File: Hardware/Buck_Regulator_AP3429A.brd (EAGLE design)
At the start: 160 x 100 mm, 23 parts, among them J2 POWER_JACKPOWER_JACK_SLOT

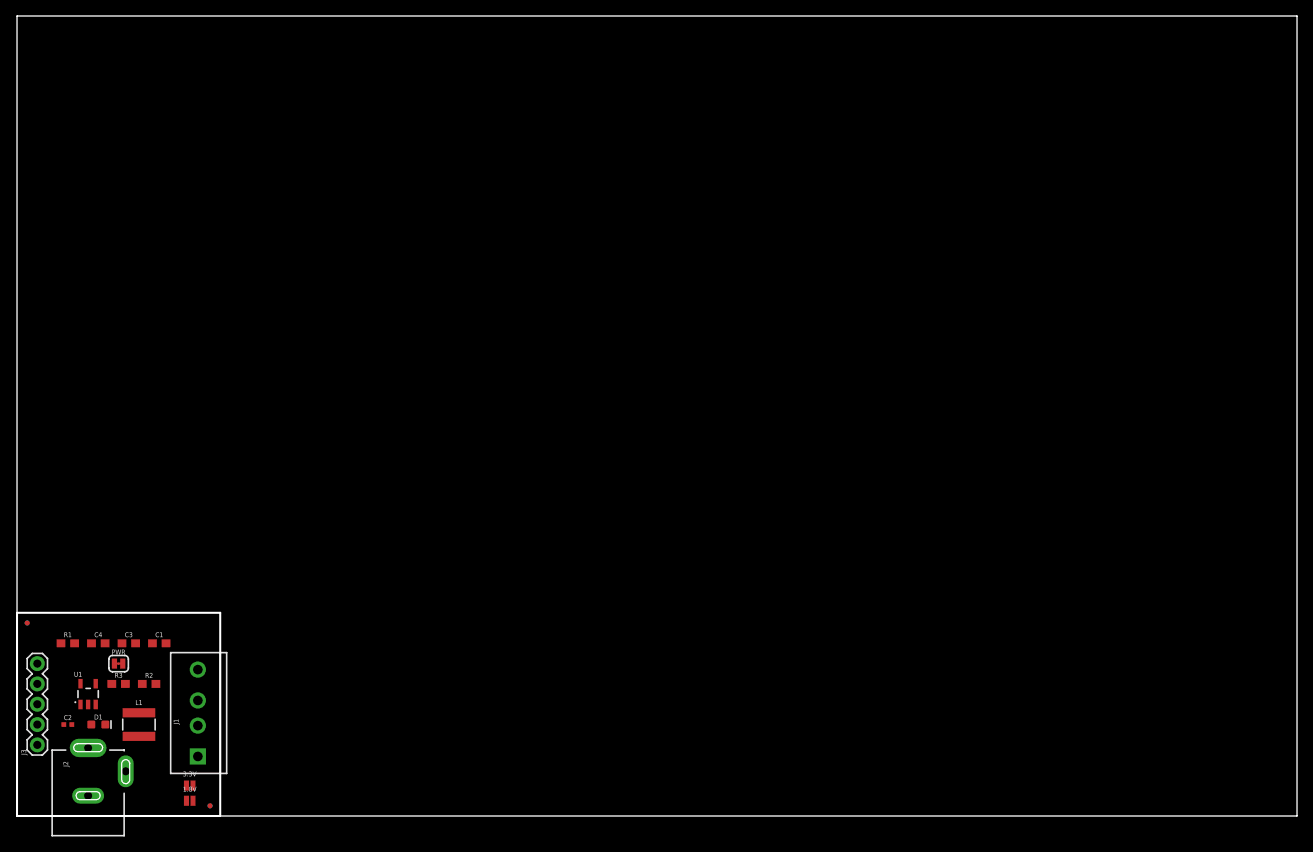
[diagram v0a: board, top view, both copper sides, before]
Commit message: Updates to project
Schematic: Changed indicator pads for soldering which version of board, added further notation, updated Power Jack device in local library.
Layout: Added power polygons and stitching vias to appropriate areas, finished routing, adjusted Power Jack to be double sided now, fixed silkscreen notation, adjusted version number, worked through design errors.
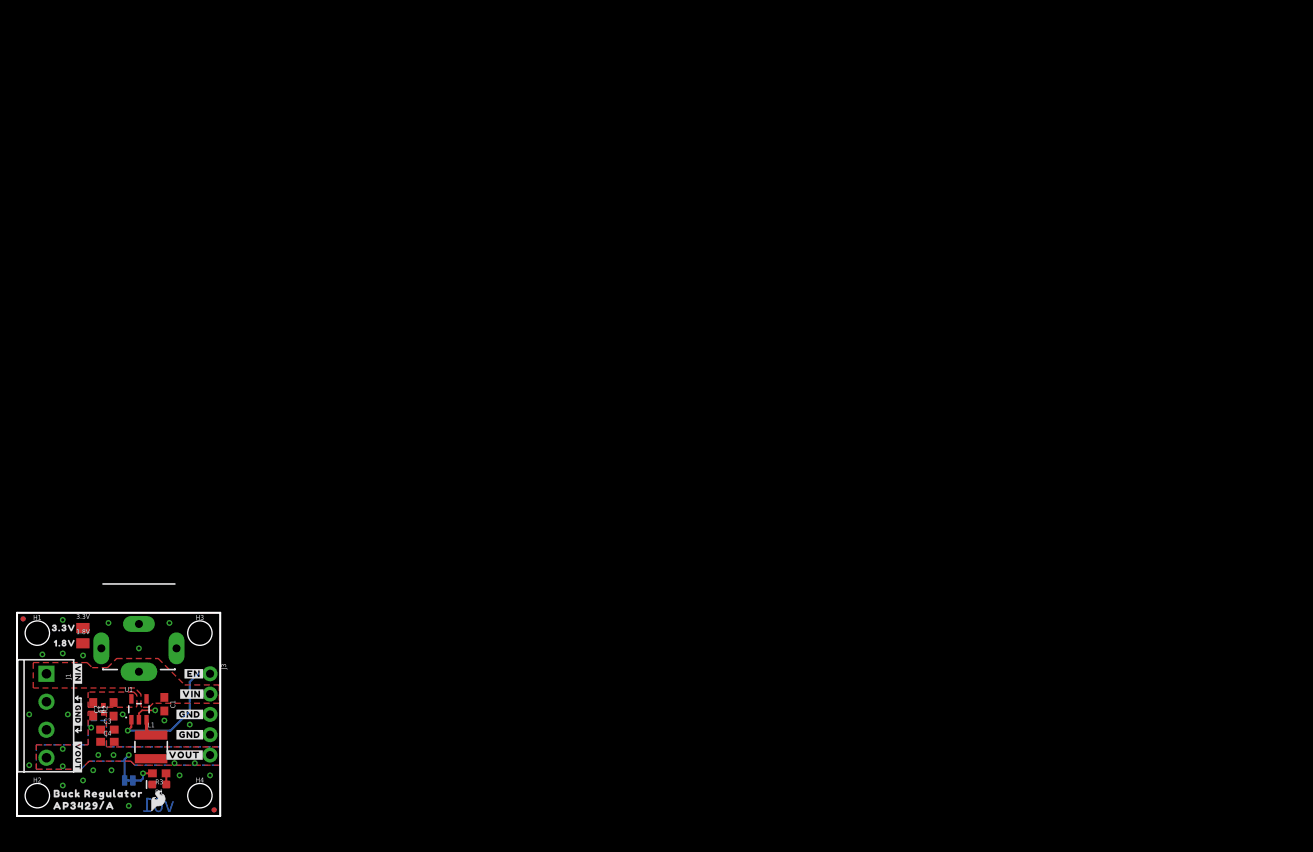
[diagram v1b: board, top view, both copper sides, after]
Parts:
- added H1, H2, H3, H4: STAND-OFFTIGHT, SparkFun-Hardware:STAND-OFF-TIGHT
- added U$1: (no value), SparkFun-Aesthetics:SFE_LOGO_FLAME_.1
- added U$10, U$11, U$15, U$16, U$5, U$6: (no value), output:#GND#3432
- added U$12, U$18, U$4: (no value), output:#VOUT#3431
- added U$13, U$17, U$7: (no value), output:#VIN#3433
- added U$14: (no value), output:#LED#3435
- added U$19: (no value), output:1#8V3436
- added U$2: (no value), output:BUCK_REGULATOR24
- added U$20: (no value), output:3#3V3436
- added U$21: (no value), output:#VOUT#3437
- added U$22: (no value), output:#VIN#3438
- added U$24: (no value), output:#GND#3439
- added U$3: (no value), output:AP3429#A25
- added U$8, U$9: (no value), output:#EN#3434
- 1.8V: value JUMPER-SMT_2_NC_PASTE_NO-SILK -> PROD_ID_PASTE_NO-SILK; device SparkFun-Jumpers:SMT-JUMPER_2_NC_PASTE_NO-SILK -> SparkFun-Aesthetics:PRODUCT_IDENT_PASTE_NO-SILK
- 3.3V: value JUMPER-SMT_2_NO_NO-SILK -> PROD_ID_NO-PASTE_NO_SILK; device SparkFun-Jumpers:SMT-JUMPER_2_NO_NO-SILK -> SparkFun-Aesthetics:PRODUCT_IDENT_NO_NO-SILK
- J1: value (none) -> Screw Terminal; device SparkFun-Connectors:SCREWTERMINAL-3.5MM-4_LOCK -> SparkFun-Connectors:SCREWTERMINAL-3.5MM-4
- J2: value POWER_JACKPOWER_JACK_SLOT -> POWER_JACKPOWER_JACK_SLOT_COMBO; device SparkFun-Connectors:POWER_JACK_PTH_SLOT -> SparkFun-Connectors:POWER_JACK_PTH_SLOT_BOTH
- J3: value (none) -> Breakout Headers; device SparkFun-Connectors:1X05 -> SparkFun-Connectors:1X05_NO_SILK
- LOGO1: value OSHW-LOGOM -> OSHW-LOGOS; device SparkFun-Aesthetics:OSHW-LOGO-M -> SparkFun-Aesthetics:OSHW-LOGO-S
- LOGO2: value SFE_LOGO_NAME_FLAME.2_INCH -> SFE_LOGO_NAME_FLAME.1_INCH; device SparkFun-Aesthetics:SFE_LOGO_NAME_FLAME_.2 -> SparkFun-Aesthetics:SFE_LOGO_NAME_FLAME_.1
- U1: value (none) -> AP3429/A
- moved 3.3V 23.8 mm to (8.26, 23.5)
- moved 1.8V 23.8 mm to (8.26, 21.6)
- moved J3 23.3 mm to (24.1, 17.8), turned to 270 degrees
- moved J2 22.4 mm to (15.2, 24.0), turned to 90 degrees
- moved J1 21.5 mm to (3.68, 17.8), turned to 270 degrees
- moved PWR 14.7 mm to (14.0, 4.45), flipped to the bottom
- moved C4 12.4 mm to (11.3, 9.27)
- moved R3 12.3 mm to (17.8, 5.33), turned to 180 degrees
- moved C3 11.1 mm to (11.3, 10.8)
- moved D1 10.7 mm to (17.8, 3.94), turned to 180 degrees
- moved R1 8.84 mm to (9.53, 13.3), turned to 270 degrees
- moved C1 7.65 mm to (18.4, 14.0), turned to 270 degrees
- moved U1 6.63 mm to (15.2, 13.3)
- moved R2 5.46 mm to (12.1, 13.3), turned to 90 degrees
- moved LOGO2 5.36 mm to (14.0, 9.02)
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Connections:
- removed net N$6: J3.3, J3.4
- removed net N$7: J1.2, J1.3
- net GND: now also J1.2, J1.3, J3.3, J3.4
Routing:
- net EN: track 0.00 -> 16.9 mm, vias 0 -> 1
- net 1.8V: track 0.00 -> 3.39 mm, vias 0 -> 8
- net N$3: track 0.00 -> 3.18 mm, vias 0 -> 1
- net GND: track 0.00 -> 2.98 mm, vias 0 -> 21
- net N$1: track 0.00 -> 2.16 mm
- net N$4: track 0.00 -> 1.41 mm
- added copper zone on layer 1, net 1.8V
- added copper zone on layer 16, net 1.8V
- added copper zone on layer 1, net GND
- added copper zone on layer 16, net GND
- added copper zone on layer 1, net N$2
- added copper zone on layer 1, net VIN
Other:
- board size 160 x 100 mm -> 25.4 x 25.4 mm
- board text added: "M. Chodikov"
- board text added: "v01"

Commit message: v01 Design Review commit
Small changes were made after running the python checklist. Added more GND vias, added the Power LED silkscreen indicator, updated dimension layer line width, adjusted polygons for better GND pour connection.
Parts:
- added U$23: (no value), output:3#3V3441
- U$19: device output:1#8V3436 -> output:1#8V3441
- U$20: device output:3#3V3436 -> output:PWR3441
- moved FRAME1 40.7 mm to (-10.2, -17.8)
- moved U$20 21.8 mm to (18.3, 5.59)
- moved U$1 8.14 mm to (10.2, 5.08)
- moved LOGO2 3.81 mm to (14.0, 12.8)
- moved U$14 2.54 mm to (13.2, 5.97)
- moved PWR 2.44 mm to (15.9, 5.97), turned to 90 degrees
- moved R3 2.22 mm to (18.3, 3.17)
- moved D1 0.72 mm to (18.3, 4.45)
- moved L1 0.46 mm to (16.5, 8.26)
- moved C3 0.25 mm to (11.3, 11.0)
- moved C4 0.25 mm to (11.3, 9.53)
- moved U$19 0.13 mm to (6.10, 21.6)
- moved R1 0.13 mm to (9.53, 13.5)
- moved R2 0.13 mm to (12.1, 13.5)
- moved U$24 0.13 mm to (7.62, 12.6)
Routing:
- net GND: track 2.98 -> 0.97 mm, vias 21 -> 20
- net 1.8V: track 3.39 -> 3.45 mm, vias 8 -> 1
- removed copper zone on layer 16, net 1.8V
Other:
- board text added: "Units in Inches"

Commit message: heat sink addition - v01 design review
Changed the SparkFun logo on the backside of the board and separated the name and flame; added an area on the backside for the heatsink to be added; adjusted silkscreen and components on backside accordingly for heatsink; moved the EN trace to the topside of the board
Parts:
- removed U$16: (no value), output:#GND#3432
- removed U$17: (no value), output:#VIN#3433
- removed U$18: (no value), output:#VOUT#3431
- added LOGO3: SFE_LOGO_FLAME.1_INCH, SparkFun-Aesthetics:SFE_LOGO_FLAME_.1
- added U$25: (no value), output:#EN#3443
- LOGO2: value SFE_LOGO_NAME_FLAME.1_INCH -> SFE_LOGO_NAME.1_INCH; device SparkFun-Aesthetics:SFE_LOGO_NAME_FLAME_.1 -> SparkFun-Aesthetics:SFE_LOGO_NAME_.1
- U$10: device output:#GND#3432 -> output:#GND#3446
- U$11: device output:#GND#3432 -> output:#VOUT#3447
- U$12: device output:#VOUT#3431 -> output:#EN#3448
- U$13: device output:#VIN#3433 -> output:#VOUT#3447
- U$15: device output:#GND#3432 -> output:#VIN#3445
- U$8: device output:#EN#3434 -> output:#GND#3446
- U$9: device output:#EN#3434 -> output:#VIN#3445
- moved U$13 18.4 mm to (5.33, 7.11), turned to 90 degrees
- moved U$14 18.0 mm to (7.62, 23.1), turned to 90 degrees
- moved U$8 17.6 mm to (5.33, 12.6), flipped to the bottom, turned to 90 degrees
- moved PWR 16.6 mm to (7.62, 20.3), turned to 270 degrees
- moved LOGO2 11.8 mm to (10.2, 1.65)
- moved U$12 10.2 mm to (22.2, 17.8)
- moved U$15 7.06 mm to (5.33, 17.8), turned to 90 degrees
- moved U$11 3.02 mm to (22.7, 7.37), turned to 270 degrees
- moved U$9 2.71 mm to (22.6, 15.1), turned to 270 degrees
- moved U$10 1.71 mm to (22.7, 11.4), turned to 270 degrees
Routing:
- net N$3: track 3.39 -> 37.4 mm
- net EN: track 16.6 -> 46.2 mm, vias 1 -> 0
- net 1.8V: track 3.45 -> 19.3 mm, vias 1 -> 0
